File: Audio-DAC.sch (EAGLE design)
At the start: 211 parts, among them CON1 USB-5075BR-04-WH, CON2 VOL_CON, CON3 SWD_CON, IC1 3.3V 200mA, IC10 15V, IC11 -15V, IC12 3.3V, IC13 LPC1114FDH28, IC14 7812, IC15 5V, IC16 5V, IC17 3.3V, IC18 TC7WH74FU, IC19 AK4495EQ, IC2 AT32UC3A3256, IC20 TC7WU04FU, IC21 9V, IC22 -9V, IC23 OP275, IC3 OCT_BUFFER-SO6, IC4 OCT_BUFFER-SO6, IC5 OCT_BUFFER-SO6, IC6 OCT_BUFFER-SO6, IC7 OCT_BUFFER-SO6, IC8 OCT_BUFFER-SO6, IC9 7805, Q1 NPN2SC3422, Q2 PNP2SA1359, Q3 NPN2SC3422, Q4 PNP2SA1359, Q5 NPN2SC3325, Q6 NPN2SC3325, SW1 EA2, SW2 EA2, X1 12MHz, X2 22.5792MHz, X3 24.576MHz

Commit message: 微修正
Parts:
- added FB3: FB-1608, my_rcl:FB-1608
- IC14: value 7812 -> 10V; device my_ic:78X-1 -> my_ic:78X-LED
- IC21: value 9V -> 10V
- IC22: value -9V -> -10V
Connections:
- new net N$56: C26.1, FB3.2, IC9.IN
- net +12V: now also FB3.1; no longer C26.1, IC9.IN
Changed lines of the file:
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@@
 <part name="SUPPLY70" library="my_supply" deviceset="GND" device=""/>
 <part name="SUPPLY71" library="my_supply" deviceset="GND" device=""/>
-<part name="IC14" library="my_ic" deviceset="78X" device="-1" value="7812"/>
+<part name="IC14" library="my_ic" deviceset="78X" device="-LED" value="10V"/>
 <part name="IC15" library="my_ic" deviceset="78X" device="-LED" value="5V"/>
 <part name="IC16" library="my_ic" deviceset="78X" device="-LED" value="5V"/>
@@
 <part name="C60" library="my_rcl" deviceset="CPOL" device="E2.5-8" value="100u"/>
 <part name="SUPPLY82" library="my_supply" deviceset="GND" device=""/>
-<part name="IC21" library="my_ic" deviceset="78X" device="-LED" value="9V"/>
-<part name="IC22" library="my_ic" deviceset="79X" device="-LED" value="-9V"/>
+<part name="IC21" library="my_ic" deviceset="78X" device="-LED" value="10V"/>
+<part name="IC22" library="my_ic" deviceset="79X" device="-LED" value="-10V"/>
 <part name="SUPPLY83" library="my_supply" deviceset="GND" device=""/>
 <part name="C40" library="my_rcl" deviceset="CPOL" device="E2.5-6.5" value="100u"/>
@@
 <part name="R26" library="my_rcl" deviceset="R" device="-1608" value="1.5k"/>
 <part name="SUPPLY132" library="my_supply" deviceset="GND" device=""/>
+<part name="FB3" library="my_rcl" deviceset="FB" device="-1608"/>
 </parts>
 <sheets>
@@
 <attribute name="VALUE" x="45.72" y="-25.4" size="1.778" layer="96"/>
 </instance>
-<instance part="P+3" gate="1" x="-180.34" y="20.32" smashed="yes">
-<attribute name="VALUE" x="-182.88" y="22.86" size="1.778" layer="96"/>
+<instance part="P+3" gate="1" x="-195.58" y="20.32" smashed="yes">
+<attribute name="VALUE" x="-198.12" y="22.86" size="1.778" layer="96"/>
 </instance>
 <instance part="CON3" gate="G$1" x="-55.88" y="-63.5" smashed="yes">
@@
 <attribute name="VALUE" x="-154.94" y="44.45" size="2.54" layer="96"/>
 </instance>
+<instance part="FB3" gate="G$1" x="-187.96" y="17.78" smashed="yes" rot="R90">
+<attribute name="NAME" x="-182.88" y="16.51" size="1.778" layer="95" rot="R180"/>
+<attribute name="VALUE" x="-182.88" y="22.86" size="1.778" layer="96" rot="R180"/>
+</instance>
 </instances>
 <busses>
@@
 </segment>
 <segment>
-<pinref part="IC9" gate="G$1" pin="IN"/>
-<wire x1="-175.26" y1="17.78" x2="-177.8" y2="17.78" width="0.1524" layer="91"/>
-<pinref part="C26" gate="G$1" pin="1"/>
-<wire x1="-177.8" y1="17.78" x2="-180.34" y2="17.78" width="0.1524" layer="91"/>
-<wire x1="-177.8" y1="15.24" x2="-177.8" y2="17.78" width="0.1524" layer="91"/>
-<junction x="-177.8" y="17.78"/>
 <pinref part="P+3" gate="1" pin="+12V"/>
+<wire x1="-193.04" y1="17.78" x2="-195.58" y2="17.78" width="0.1524" layer="91"/>
+<pinref part="FB3" gate="G$1" pin="1"/>
 </segment>
 </net>
@@
 </segment>
 </net>
+<net name="N$56" class="0">
+<segment>
+<pinref part="IC9" gate="G$1" pin="IN"/>
+<wire x1="-175.26" y1="17.78" x2="-177.8" y2="17.78" width="0.1524" layer="91"/>
+<pinref part="C26" gate="G$1" pin="1"/>
+<wire x1="-177.8" y1="15.24" x2="-177.8" y2="17.78" width="0.1524" layer="91"/>
+<junction x="-177.8" y="17.78"/>
+<wire x1="-177.8" y1="17.78" x2="-182.88" y2="17.78" width="0.1524" layer="91"/>
+<pinref part="FB3" gate="G$1" pin="2"/>
+</segment>
+</net>

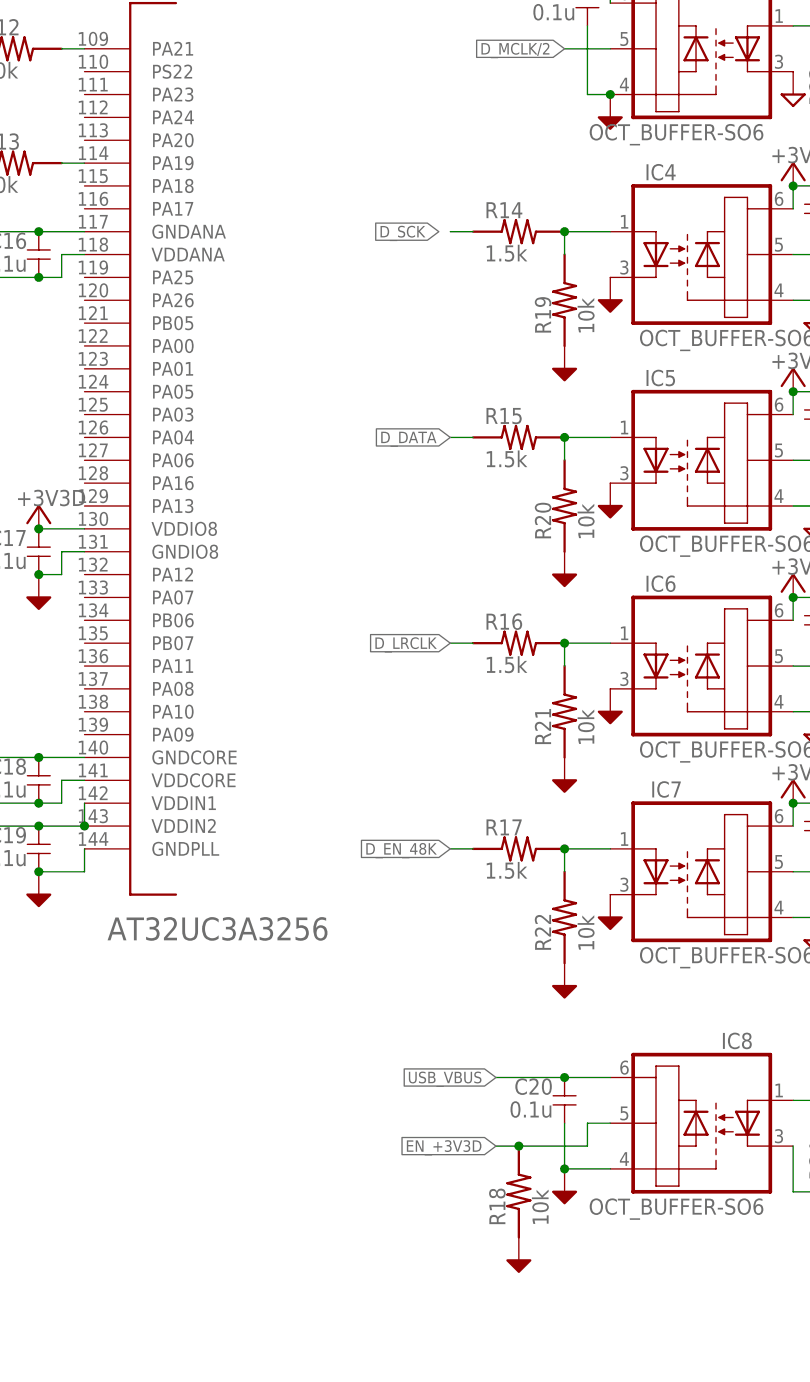
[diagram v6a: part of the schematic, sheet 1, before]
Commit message: フォトカプラを反転
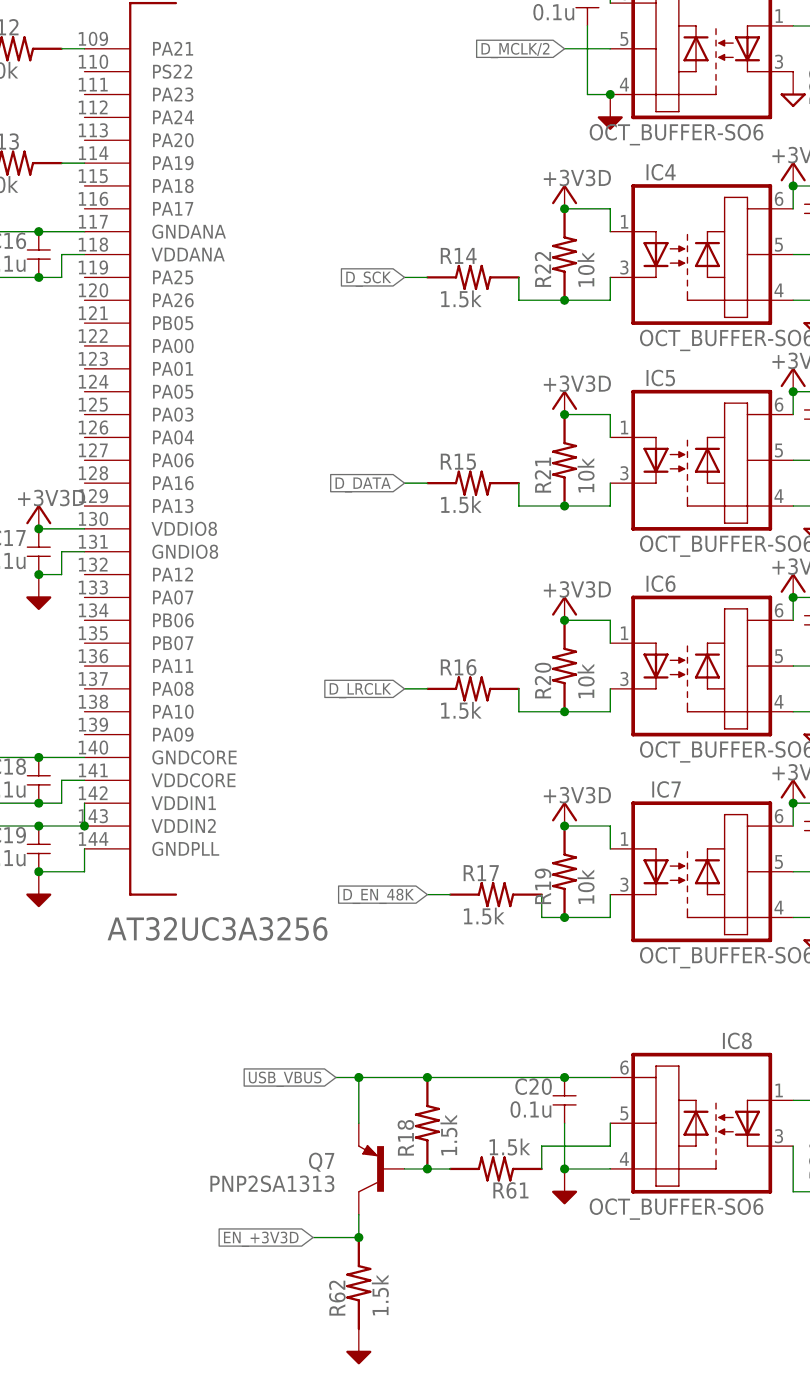
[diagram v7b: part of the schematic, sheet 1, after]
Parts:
- added Q7: PNP2SA1313, my_ic:PNP2SA1313
- added R61, R62: 1.5k, my_rcl:R-1608
- R18: value 10k -> 1.5k
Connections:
- new net N$58: IC6.C, R16.2, R20.1
- new net N$61: IC7.C, R17.2, R19.1
- net +3V3D: now also IC4.A, IC5.A, IC6.A, IC7.A, R19.2, R20.2, R21.2, R22.2
- net DGND: now also R62.1; no longer IC4.C, IC5.C, IC6.C, IC7.C, R18.1, R19.1, R20.1, R21.1, R22.1
- net EN_+3V3D: now also Q7.C, R62.2; no longer IC8.OUT, R18.2
- net N$14: now also Q7.B, R18.1, R61.2; no longer IC7.A, R17.2, R22.2
- net N$15: now also IC4.C, R22.1; no longer IC4.A, R19.2
- net N$16: now also IC8.OUT, R61.1; no longer IC5.A, R15.2, R20.2
- net N$17: now also IC5.C, R15.2, R21.1; no longer IC6.A, R16.2, R21.2
- net USB_VBUS: now also Q7.E, R18.2
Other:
- moved on the sheet: R14, R15, R16, R17, R18, R19, R20, R21, R22

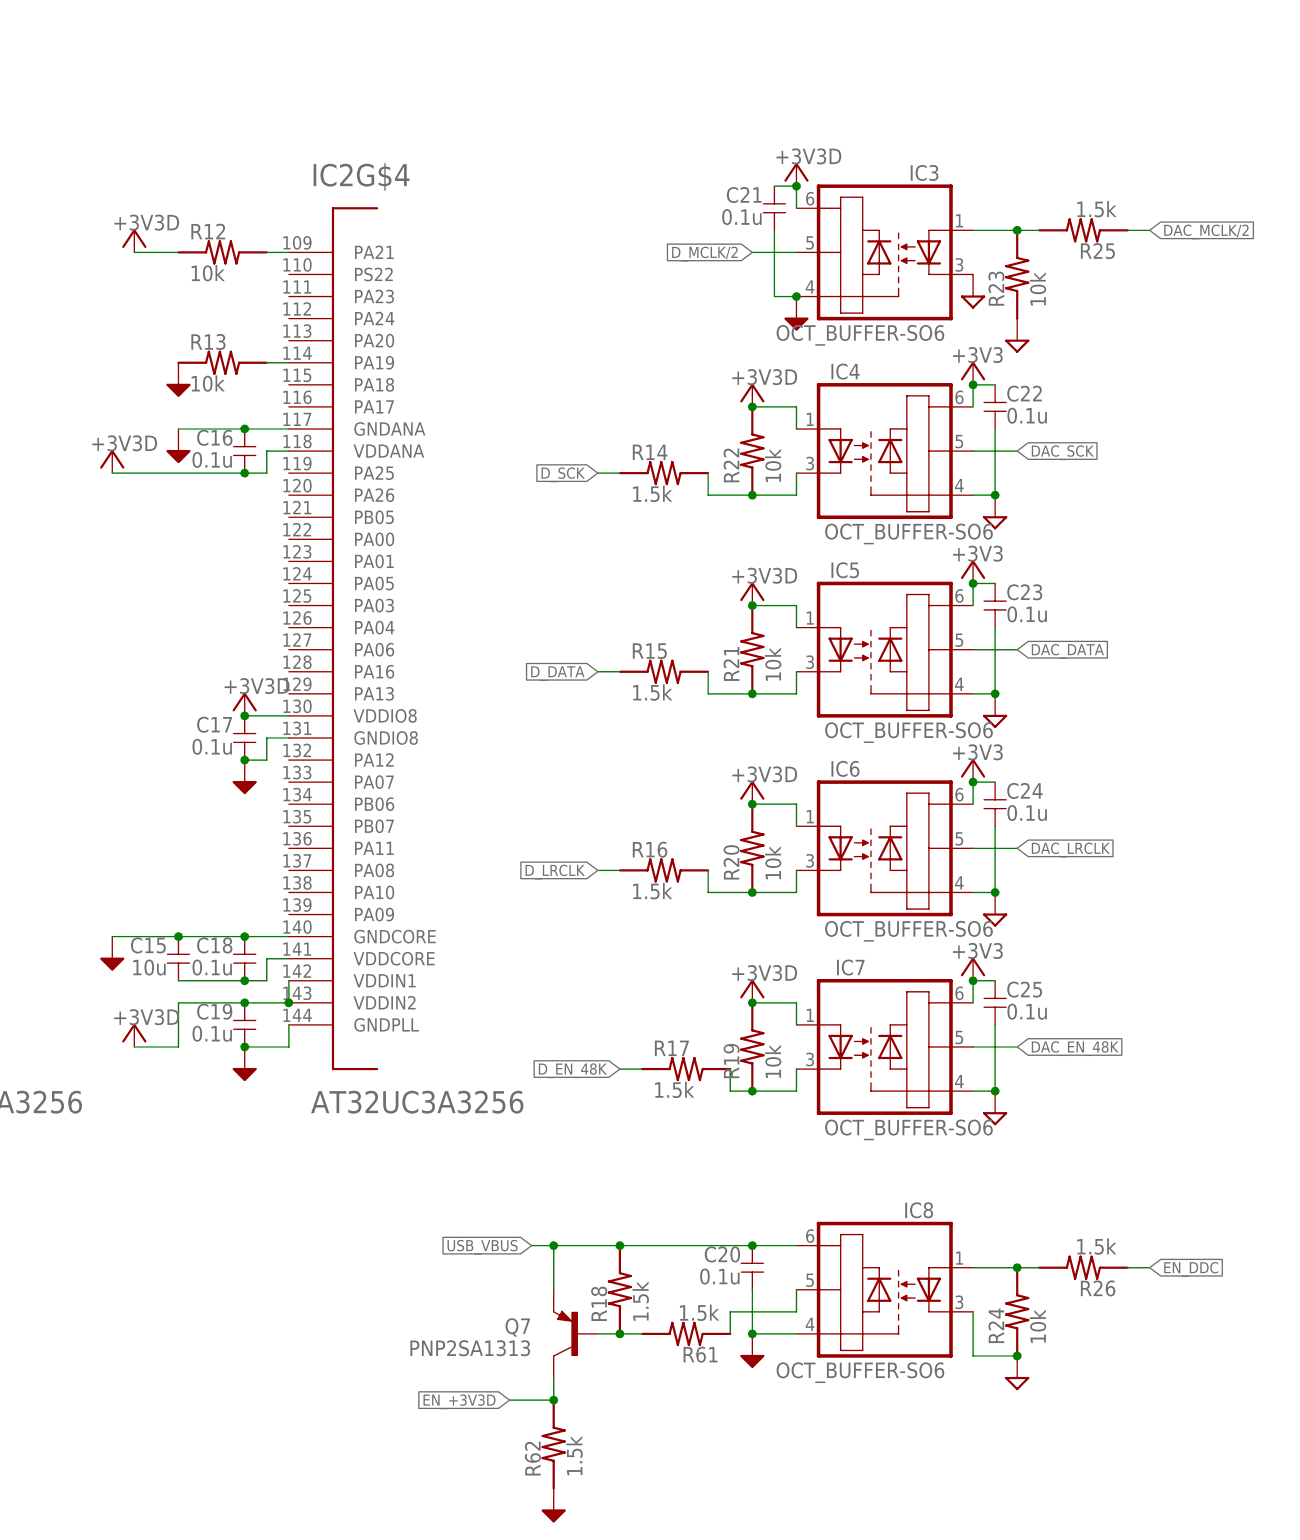
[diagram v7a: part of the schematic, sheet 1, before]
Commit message: アイソレーターをsi8420に
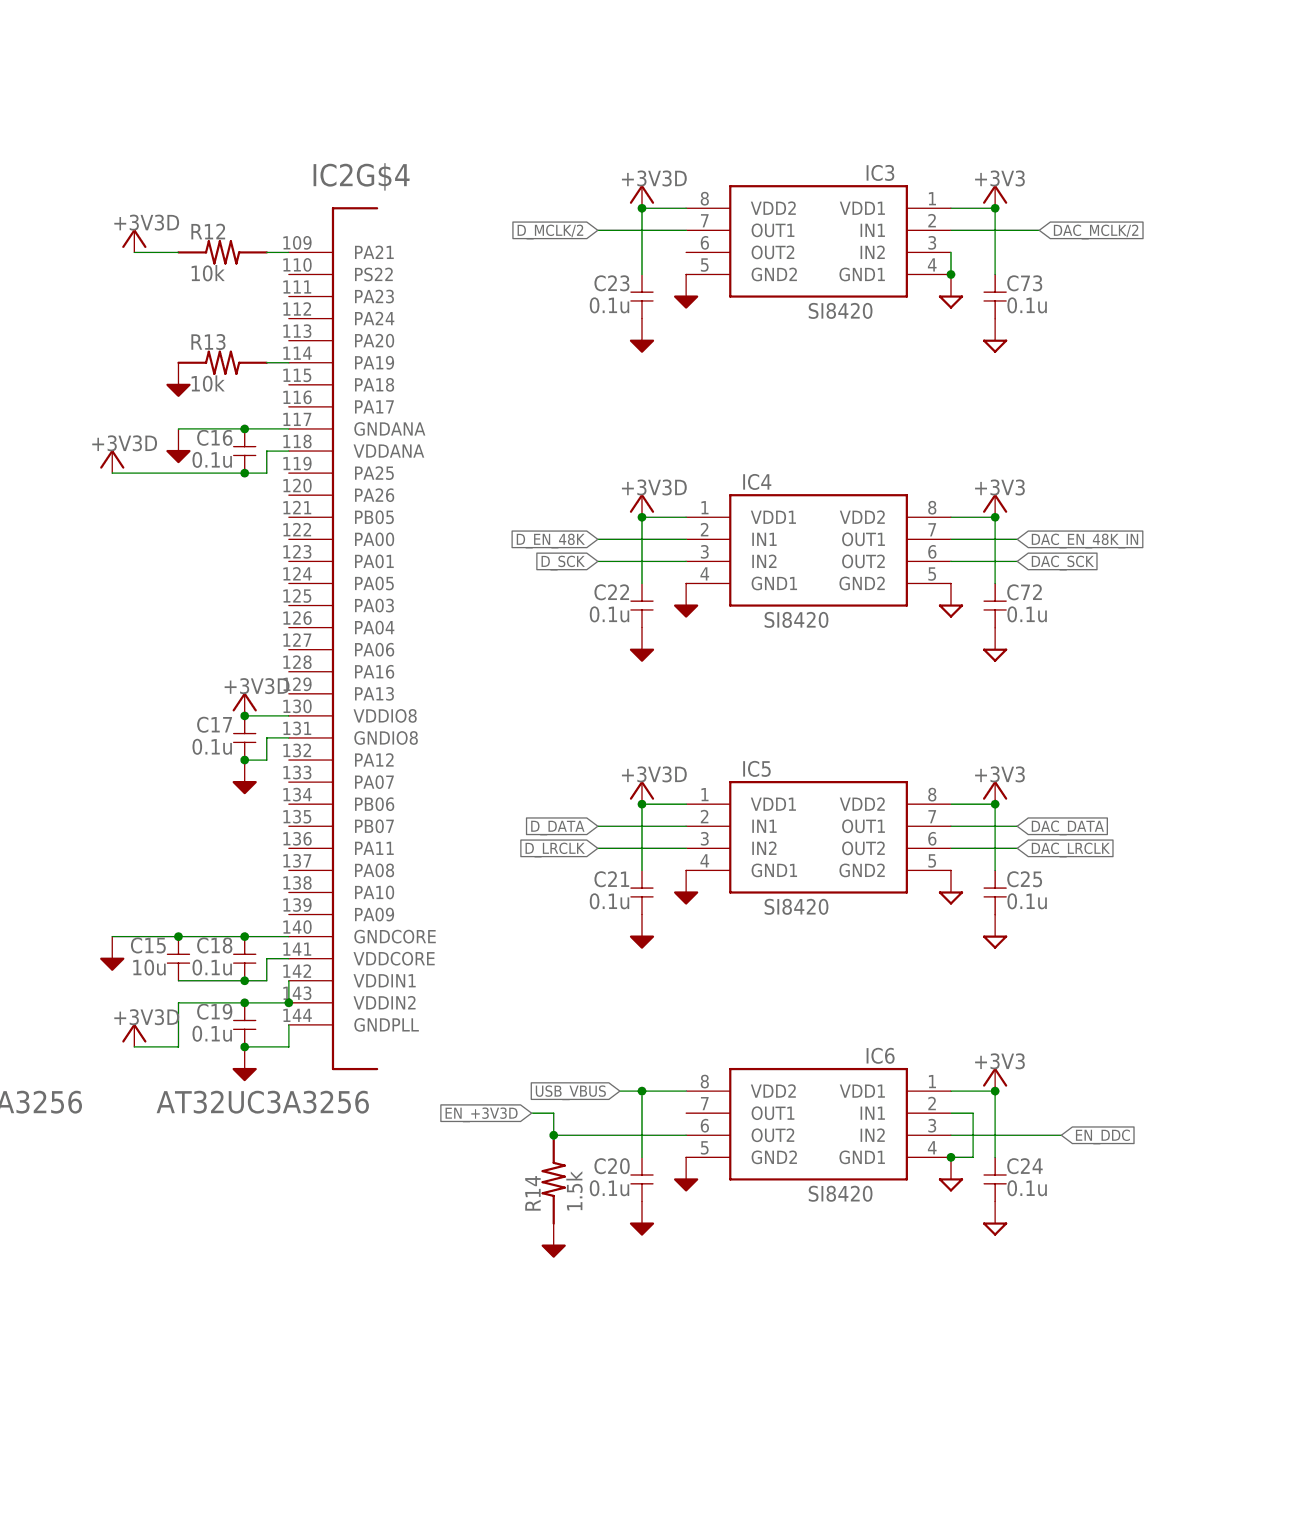
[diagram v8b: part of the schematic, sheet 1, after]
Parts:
- removed IC7, IC8: OCT_BUFFER-SO6, my_ic:OCT_BUFFER-SO6
- removed Q7: PNP2SA1313, my_ic:PNP2SA1313
- removed R15, R16, R17, R18, R25, R26, R61, R62: 1.5k, my_rcl:R-1608
- removed R19, R20, R21, R22, R23, R24: 10k, my_rcl:R-1608
- added C72, C73: 0.1u, my_rcl:C-1608
- IC3, IC4, IC5, IC6: value OCT_BUFFER-SO6 -> SI8420; device my_ic:OCT_BUFFER-SO6 -> my_ic:SI8420
- X2: value 22.5792MHz -> 24.576MHz
- X3: value 24.576MHz -> 22.5792MHz
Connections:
- removed net N$14: Q7.B, R18.1, R61.2
- removed net N$15: IC4.C, R14.2, R22.1
- removed net N$16: IC8.OUT, R61.1
- removed net N$17: IC5.C, R15.2, R21.1
- removed net N$19: IC3.A, R23.2, R25.2
- removed net N$55: IC8.A, R24.2, R26.2
- removed net N$58: IC6.C, R16.2, R20.1
- removed net N$61: IC7.C, R17.2, R19.1
- new net DAC_EN_48K_IN: IC20G$1.P$1, IC4.OUT1
- net +3V3: now also C72.1, C73.1, IC3.VDD1, IC4.VDD2, IC5.VDD2, IC6.VDD1; no longer C22.1, C23.1, IC20G$2.P$1, IC4.V+, IC5.V+, IC6.V+, IC7.V+
- net +3V3D: now also C22.1, C23.1, IC3.VDD2, IC4.VDD1, IC5.VDD1; no longer IC3.V+, IC4.A, IC5.A, IC6.A, IC7.A, R19.2, R20.2, R21.2, R22.2
- net DAC_!EN_48K: now also IC20G$3.P$1, X3.EN; no longer X2.EN
- net DAC_DATA: now also IC5.OUT1; no longer IC5.OUT
- net DAC_EN_48K: now also IC20G$3.P$2, X2.EN; no longer IC20G$1.P$1, IC7.OUT, X3.EN
- net DAC_LRCLK: now also IC5.OUT2; no longer IC6.OUT
- net DAC_MCLK/2: now also IC3.IN1; no longer R25.1
- net DAC_SCK: now also IC4.OUT2; no longer IC4.OUT
- net DGND: now also C22.2, C23.2, IC3.GND2, IC4.GND1, IC5.GND1, IC6.GND2, R14.1; no longer IC3.GND, IC8.GND, R62.1
- net D_DATA: now also IC5.IN1; no longer R15.1
- net D_EN_48K: now also IC4.IN1; no longer R17.1
- net D_LRCLK: now also IC5.IN2; no longer R16.1
- net D_MCLK/2: now also IC3.OUT1; no longer IC3.OUT
- net D_SCK: now also IC4.IN2; no longer R14.1
- net EN_+3V3D: now also IC6.OUT2, R14.2; no longer Q7.C, R62.2
- net EN_DDC: now also IC6.IN2; no longer R26.1
- net GND: now also C72.2, C73.2, IC20G$2.P$1, IC3.GND1, IC3.IN2, IC4.GND2, IC5.GND2, IC6.GND1, IC6.IN1; no longer C22.2, C23.2, IC20G$3.P$1, IC3.C, IC4.GND, IC5.GND, IC6.GND, IC7.GND, IC8.C, R23.1, R24.1
- net USB_VBUS: now also IC6.VDD2; no longer IC8.V+, Q7.E, R18.2
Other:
- moved on the sheet: C20, C21, C22, C23, C24, C25, IC20G$2, R14
